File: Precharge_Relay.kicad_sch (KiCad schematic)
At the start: 7 parts, among them K3 G9EJH-1-E, Q7 DMN61D8LQ, Q8 DMN61D8LQ

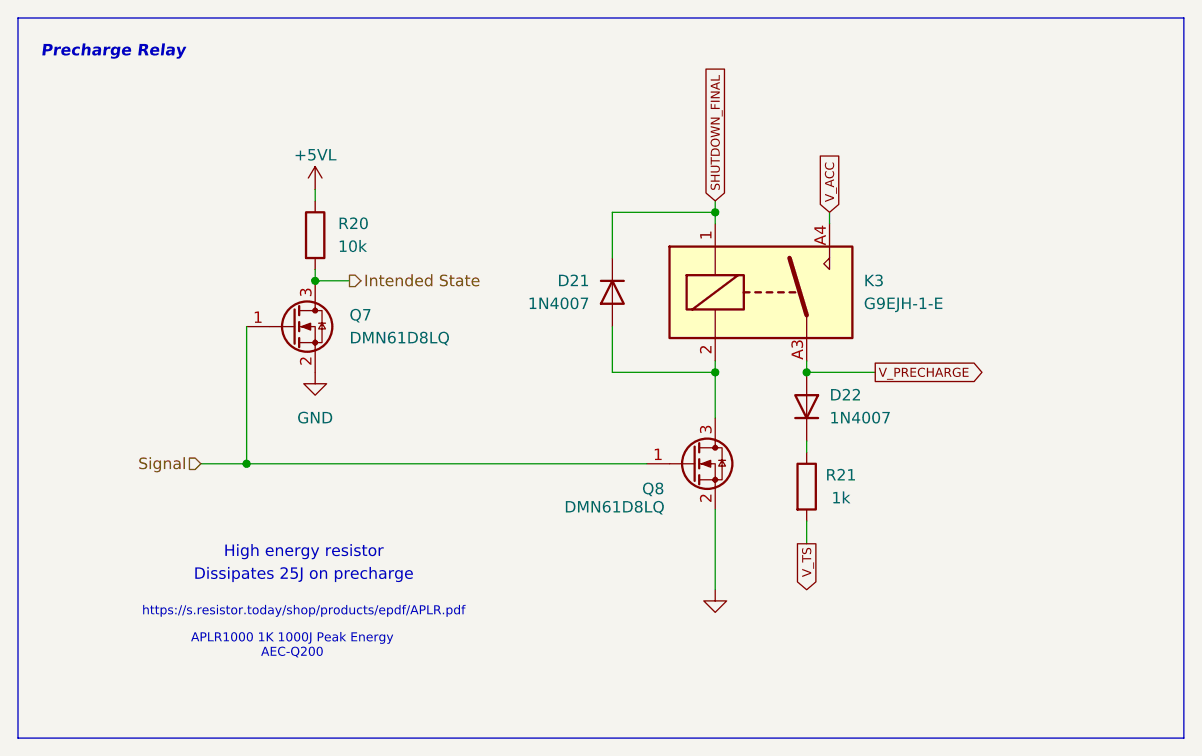
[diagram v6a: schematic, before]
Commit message: schematic: Add zener diode across precharge relay
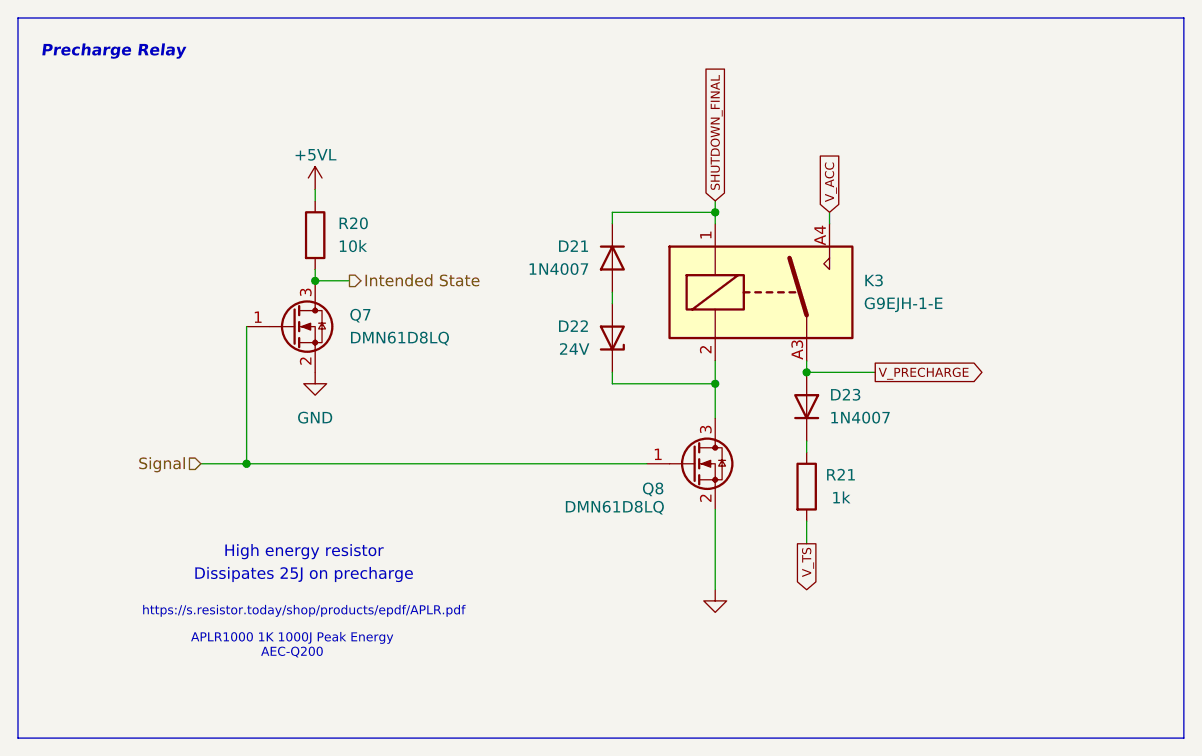
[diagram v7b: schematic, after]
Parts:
- added D22: 24V, Diode_SMD:D_SMA, symbol Device:D_Zener
- renumbered D22 to D23
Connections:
- net at K3.2, Q8.3 (D): now also D22.1 (K); no longer D21.2 (A)
- new net: D21.2 (A), D22.2 (A)
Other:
- moved on the sheet: D21
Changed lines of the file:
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@@
+	)
+	(junction
+		(at 110.49 74.93)
+		(diameter 0)
+		(color 0 0 0 0)
 	)
 	(junction
@@
 	)
 	(junction
-		(at 110.49 73.66)
-		(diameter 0)
-		(color 0 0 0 0)
-	)
-	(junction
 		(at 110.49 55.88)
 		(diameter 0)
@@
 	(wire
 		(pts
+			(xy 110.49 55.88) (xy 110.49 57.15)
+		)
+		(stroke
+			(width 0)
+			(type default)
+		)
+	)
+	(wire
+		(pts
 			(xy 53.34 83.82) (xy 58.42 83.82)
 		)
@@
 	(wire
 		(pts
-			(xy 110.49 73.66) (xy 110.49 78.74)
+			(xy 110.49 72.39) (xy 110.49 74.93)
 		)
 		(stroke
@@
 	(wire
 		(pts
-			(xy 99.06 55.88) (xy 99.06 60.96)
-		)
-		(stroke
-			(width 0)
-			(type default)
-		)
-	)
-	(wire
-		(pts
 			(xy 58.42 68.58) (xy 58.42 83.82)
 		)
@@
 	(wire
 		(pts
-			(xy 99.06 68.58) (xy 99.06 73.66)
+			(xy 99.06 74.93) (xy 110.49 74.93)
+		)
+		(stroke
+			(width 0)
+			(type default)
+		)
+	)
+	(wire
+		(pts
+			(xy 128.27 73.66) (xy 120.65 73.66)
+		)
+		(stroke
+			(width 0)
+			(type default)
+		)
+	)
+	(wire
+		(pts
+			(xy 99.06 55.88) (xy 99.06 57.15)
+		)
+		(stroke
+			(width 0)
+			(type default)
+		)
+	)
+	(wire
+		(pts
+			(xy 120.65 92.71) (xy 120.65 90.17)
 		)
 		(stroke
@@
 	(wire
 		(pts
-			(xy 99.06 73.66) (xy 110.49 73.66)
-		)
-		(stroke
-			(width 0)
-			(type default)
-		)
-	)
-	(wire
-		(pts
-			(xy 128.27 73.66) (xy 120.65 73.66)
-		)
-		(stroke
-			(width 0)
-			(type default)
-		)
-	)
-	(wire
-		(pts
-			(xy 120.65 92.71) (xy 120.65 90.17)
-		)
-		(stroke
-			(width 0)
-			(type default)
-		)
-	)
-	(wire
-		(pts
-			(xy 110.49 55.88) (xy 110.49 57.15)
-		)
-		(stroke
-			(width 0)
-			(type default)
-		)
-	)
-	(wire
-		(pts
 			(xy 120.65 82.55) (xy 120.65 81.28)
 		)
@@
 	(wire
 		(pts
+			(xy 110.49 74.93) (xy 110.49 78.74)
+		)
+		(stroke
+			(width 0)
+			(type default)
+		)
+	)
+	(wire
+		(pts
 			(xy 120.65 73.66) (xy 120.65 72.39)
 		)
@@
 	(wire
 		(pts
-			(xy 110.49 72.39) (xy 110.49 73.66)
+			(xy 99.06 64.77) (xy 99.06 66.04)
+		)
+		(stroke
+			(width 0)
+			(type default)
+		)
+	)
+	(wire
+		(pts
+			(xy 99.06 73.66) (xy 99.06 74.93)
 		)
 		(stroke
@@
 	(symbol
 		(lib_id "Diode:1N4007")
-		(at 99.06 64.77 90)
+		(at 99.06 60.96 90)
 		(mirror x)
 		(unit 1)
@@
 		(dnp no)
 		(property "Reference" "D21"
-			(at 96.52 63.4999 90)
+			(at 96.52 59.6899 90)
 			(effects
 				(font
@@
 		)
 		(property "Value" "1N4007"
-			(at 96.52 66.0399 90)
+			(at 96.52 62.2299 90)
 			(effects
 				(font
@@
 		)
 		(property "Footprint" "Diode_SMD:D_SMA"
-			(at 103.505 64.77 0)
+			(at 103.505 60.96 0)
 			(effects
 				(font
@@
 		)
 		(property "Datasheet" "http://www.vishay.com/docs/88503/1n4001.pdf"
-			(at 99.06 64.77 0)
+			(at 99.06 60.96 0)
 			(effects
 				(font
@@
 		)
 		(property "Description" "1000V 1A General Purpose Rectifier Diode, DO-41"
-			(at 99.06 64.77 0)
+			(at 99.06 60.96 0)
 			(effects
 				(font
@@
 		)
 		(property "Sim.Device" "D"
-			(at 99.06 64.77 0)
+			(at 99.06 60.96 0)
 			(effects
 				(font
@@
 		)
 		(property "Sim.Pins" "1=K 2=A"
-			(at 99.06 64.77 0)
+			(at 99.06 60.96 0)
 			(effects
 				(font
@@
 		(on_board yes)
 		(dnp no)
-		(property "Reference" "D22"
+		(property "Reference" "D23"
 			(at 123.19 76.2 90)
 			(effects
@@
 			(project "Precharge_PCB"
 				(path "/c467677d-b98c-4488-bd11-965ef67263b2/c2fa71c2-1bd3-4dc0-8faf-814cfbc0b0db"
-					(reference "D22")
+					(reference "D23")
 					(unit 1)
 				)
@@
 					(unit 1)
 				)
+			)
+		)
+	)
+	(symbol
+		(lib_id "Device:D_Zener")
+		(at 99.06 69.85 270)
+		(mirror x)
+		(unit 1)
+		(exclude_from_sim no)
+		(in_bom yes)
+		(on_board yes)
+		(dnp no)
+		(property "Reference" "D22"
+			(at 96.52 68.5799 90)
+			(effects
+				(font
+					(size 1.27 1.27)
+				)
+				(justify right)
+			)
+		)
+		(property "Value" "24V"
+			(at 96.52 71.1199 90)
+			(effects
+				(font
+					(size 1.27 1.27)
+				)
+				(justify right)
+			)
+		)
+		(property "Footprint" "Diode_SMD:D_SMA"
+			(at 99.06 69.85 0)
+			(effects
+				(font
+					(size 1.27 1.27)
+				)
+				(hide yes)
+			)
+		)
+		(property "Datasheet" "~"
+			(at 99.06 69.85 0)
+			(effects
+				(font
+					(size 1.27 1.27)
+				)
+				(hide yes)
+			)
+		)
+		(property "Description" "Zener diode"
+			(at 99.06 69.85 0)
+			(effects
+				(font
+					(size 1.27 1.27)
+				)
+				(hide yes)
+			)
+		)
+		(pin "2"
+		)
+		(pin "1"
+		)
+		(instances
+			(project ""
+				(path "/c467677d-b98c-4488-bd11-965ef67263b2/c2fa71c2-1bd3-4dc0-8faf-814cfbc0b0db"
+					(reference "D22")
+					(unit 1)
+				)

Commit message: schematic: Add BOM entries for precharge relay and associated zener
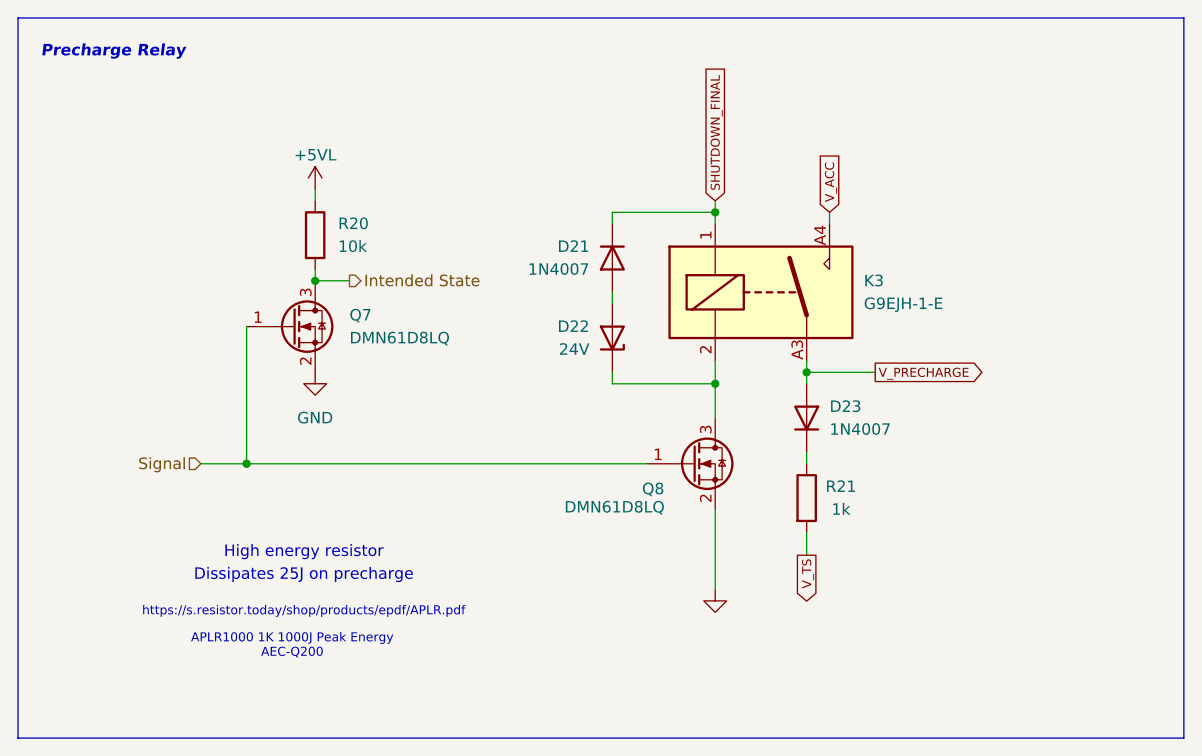
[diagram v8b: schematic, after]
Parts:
- D22: Dist (none) -> DigiKey; Dist # (none) -> BZG05C24-M3-08GICT-ND; Mfr (none) -> VISHAY; Mfr # (none) -> BZG05C24-M3-08
- K3: Dist (none) -> DigiKey; Dist # (none) -> 39-G9EJH-1-P-EDC12-ND; Mfr (none) -> Omron; Mfr # (none) -> G9EJH-1-P-E DC12
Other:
- moved on the sheet: D23, R21
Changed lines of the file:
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@@
+	(wire
+		(pts
+			(xy 120.65 74.93) (xy 120.65 73.66)
+		)
+		(stroke
+			(width 0)
+			(type default)
+		)
+	)
 	(wire
 		(pts
@@
 	(wire
 		(pts
-			(xy 120.65 92.71) (xy 120.65 90.17)
+			(xy 120.65 93.98) (xy 120.65 91.44)
 		)
 		(stroke
@@
 	(wire
 		(pts
-			(xy 120.65 82.55) (xy 120.65 81.28)
+			(xy 120.65 83.82) (xy 120.65 82.55)
 		)
 		(stroke
@@
 	(global_label "V_TS"
 		(shape output)
-		(at 120.65 92.71 270)
+		(at 120.65 93.98 270)
 		(fields_autoplaced yes)
 		(effects
@@
 		)
 		(property "Intersheetrefs" "${INTERSHEET_REFS}"
-			(at 120.65 98.3936 90)
+			(at 120.65 99.6636 90)
 			(effects
 				(font
@@
 	(symbol
 		(lib_id "Diode:1N4007")
-		(at 120.65 77.47 270)
+		(at 120.65 78.74 270)
 		(mirror x)
 		(unit 1)
@@
 		(dnp no)
 		(property "Reference" "D23"
-			(at 123.19 76.2 90)
+			(at 123.19 77.47 90)
 			(effects
 				(font
@@
 		)
 		(property "Value" "1N4007"
-			(at 123.19 78.74 90)
+			(at 123.19 80.01 90)
 			(effects
 				(font
@@
 		)
 		(property "Footprint" "Diode_SMD:D_SMA"
-			(at 116.205 77.47 0)
+			(at 116.205 78.74 0)
 			(effects
 				(font
@@
 		)
 		(property "Datasheet" "http://www.vishay.com/docs/88503/1n4001.pdf"
-			(at 120.65 77.47 0)
+			(at 120.65 78.74 0)
 			(effects
 				(font
@@
 		)
 		(property "Description" "1000V 1A General Purpose Rectifier Diode, DO-41"
-			(at 120.65 77.47 0)
+			(at 120.65 78.74 0)
 			(effects
 				(font
@@
 		)
 		(property "Sim.Device" "D"
-			(at 120.65 77.47 0)
+			(at 120.65 78.74 0)
 			(effects
 				(font
@@
 		)
 		(property "Sim.Pins" "1=K 2=A"
-			(at 120.65 77.47 0)
+			(at 120.65 78.74 0)
 			(effects
 				(font
@@
 	(symbol
 		(lib_id "Device:R")
-		(at 120.65 86.36 0)
+		(at 120.65 87.63 0)
 		(unit 1)
 		(exclude_from_sim no)
@@
 		(dnp no)
 		(property "Reference" "R21"
-			(at 124.46 85.09 0)
+			(at 124.46 86.36 0)
 			(effects
 				(font
@@
 		)
 		(property "Value" "1k"
-			(at 124.46 87.63 0)
+			(at 124.46 88.9 0)
 			(effects
 				(font
@@
 		)
 		(property "Footprint" "yfs:APLR1000"
-			(at 118.872 86.36 90)
+			(at 118.872 87.63 90)
 			(effects
 				(font
@@
 		)
 		(property "Datasheet" "https://s.resistor.today/shop/products/epdf/APLR.pdf"
-			(at 120.65 86.36 0)
+			(at 120.65 87.63 0)
 			(effects
 				(font
@@
 		)
 		(property "Description" "Non-Inductive High Energy Anti-Pulse Resistor"
-			(at 120.65 86.36 0)
+			(at 120.65 87.63 0)
 			(effects
 				(font
@@
 		)
 		(property "Dist" "DigiKey"
-			(at 120.65 86.36 0)
+			(at 120.65 87.63 0)
 			(effects
 				(font
@@
 		)
 		(property "Dist #" "4506-APLR1000J1K00SE-ND"
-			(at 120.65 86.36 0)
+			(at 120.65 87.63 0)
 			(effects
 				(font
@@
 		)
 		(property "Mfr" "C&B/RESI"
-			(at 120.65 86.36 0)
+			(at 120.65 87.63 0)
 			(effects
 				(font
@@
 		)
 		(property "Mfr #" "APLR1000J1K00SE"
-			(at 120.65 86.36 0)
+			(at 120.65 87.63 0)
 			(effects
 				(font
@@
 			)
 		)
+		(property "Dist" "DigiKey"
+			(at 115.57 64.77 0)
+			(effects
+				(font
+					(size 1.27 1.27)
+				)
+				(hide yes)
+			)
+		)
+		(property "Dist #" "39-G9EJH-1-P-EDC12-ND"
+			(at 115.57 64.77 0)
+			(effects
+				(font
+					(size 1.27 1.27)
+				)
+				(hide yes)
+			)
+		)
+		(property "Mfr" "Omron"
+			(at 115.57 64.77 0)
+			(effects
+				(font
+					(size 1.27 1.27)
+				)
+				(hide yes)
+			)
+		)
+		(property "Mfr #" "G9EJH-1-P-E DC12"
+			(at 115.57 64.77 0)
+			(effects
+				(font
+					(size 1.27 1.27)
+				)
+				(hide yes)
+			)
+		)
 		(pin "A4"
 		)
@@
 			(effects
 				(font
+					(size 1.27 1.27)
+				)
+				(hide yes)
+			)
+		)
+		(property "Dist" "DigiKey"
+			(at 99.06 69.85 90)
+			(effects
+				(font
+					(size 1.27 1.27)
+				)
+				(hide yes)
+			)
+		)
+		(property "Dist #" "BZG05C24-M3-08GICT-ND"
+			(at 99.06 69.85 90)
+			(effects
+				(font
+					(size 1.27 1.27)
+				)
+				(hide yes)
+			)
+		)
+		(property "Mfr" "VISHAY"
+			(at 99.06 69.85 90)
+			(effects
+				(font
+					(size 1.27 1.27)
+				)
+				(hide yes)
+			)
+		)
+		(property "Mfr #" "BZG05C24-M3-08"
+			(at 99.06 69.85 90)
+			(effects
+				(font
